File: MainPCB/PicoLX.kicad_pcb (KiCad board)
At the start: 2 copper layers, 120.6 x 70.6 mm, 83 parts, among them J1 USB_C_Receptacle_USB2.0, J2 Conn_01x03, SW1 SW_Push, U1 RP2040, U2 W25Q32JVSS, U3 NCP1117-3.3_SOT223, U4 SN74LV1T34DBV, Y1 12.000MHz

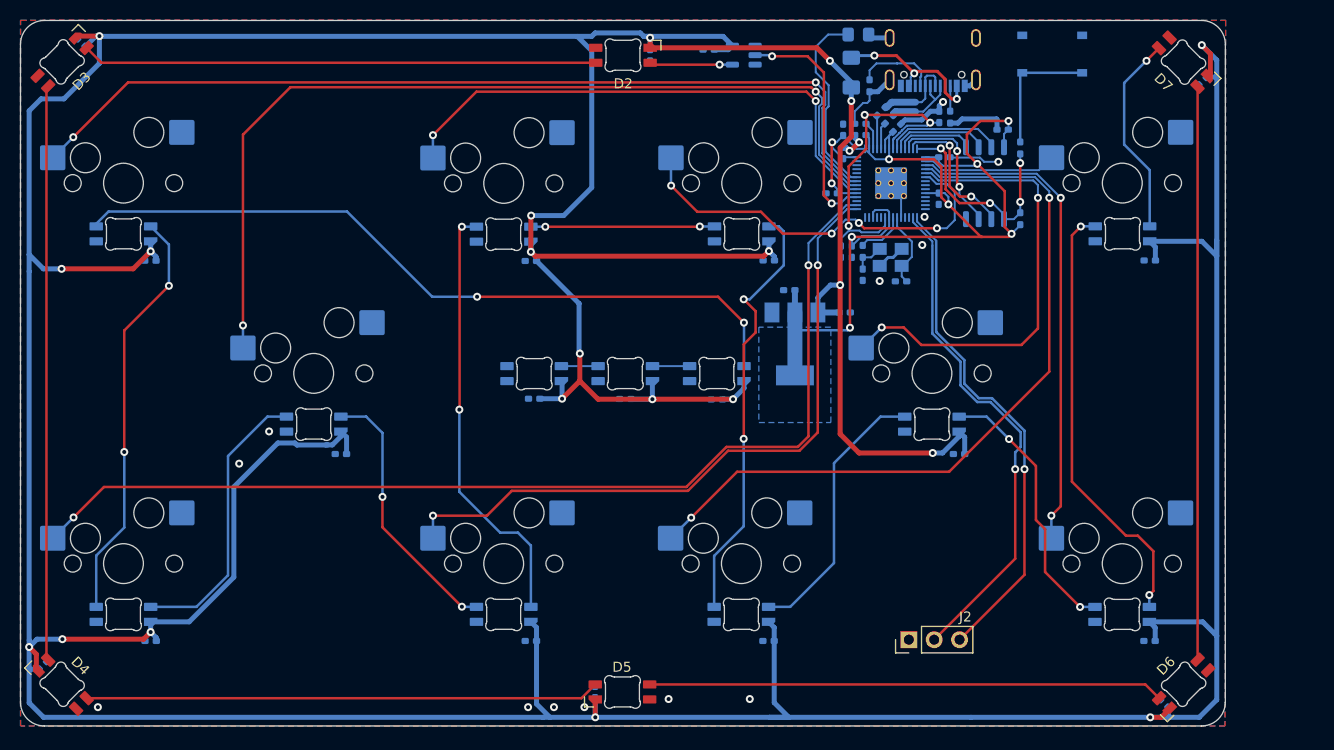
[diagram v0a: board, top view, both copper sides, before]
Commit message: fancy plate graphics, reroute all the LEDs because wrong pinout
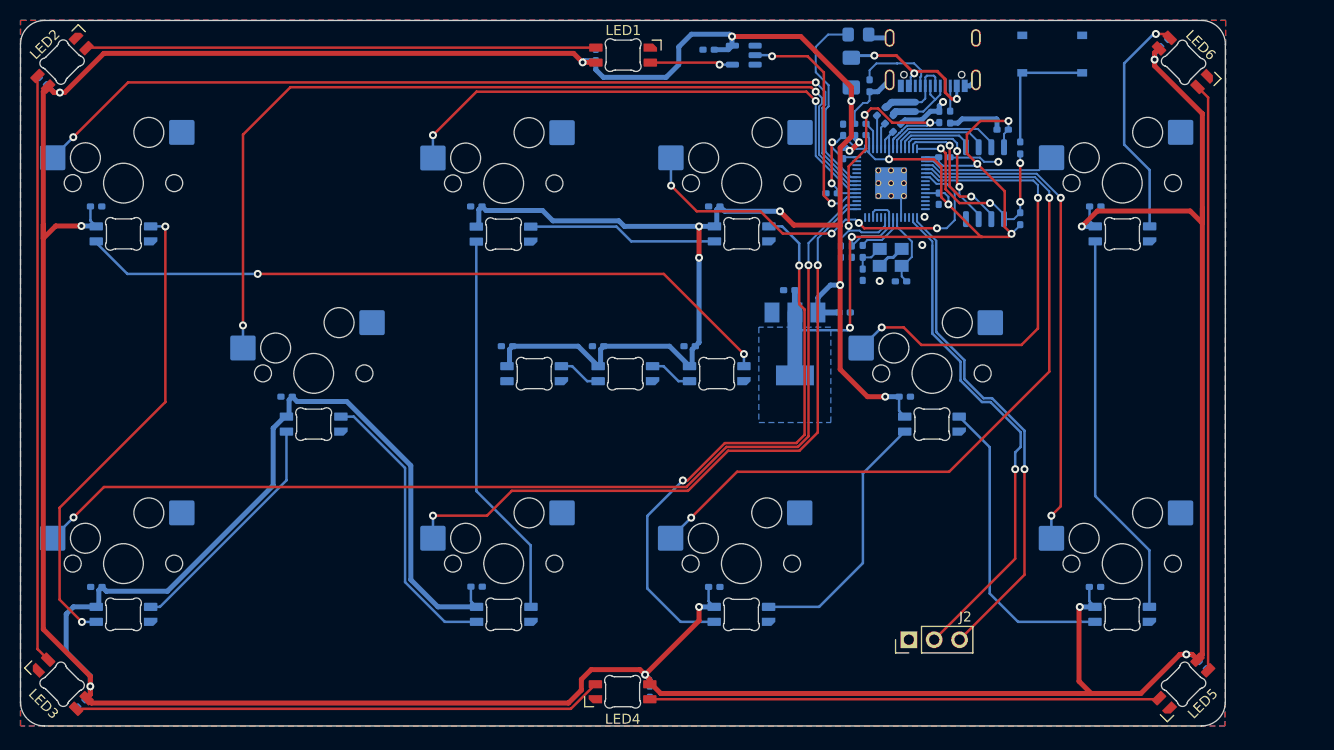
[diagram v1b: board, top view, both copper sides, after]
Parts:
- removed D10, D11, D12, D13, D14, D15, D16, D17, D18, D19, D2, D20, D3, D4, D5, D6, D7, D8, D9: SK6812MINI, marbastlib-various:LED_6028R
- added LED1: SK6812MINI-E, marbastlib-various:LED_6028R, F.Cu at (159.4, 64.5)
- added LED10: SK6812MINI-E, marbastlib-various:LED_6028R, B.Cu at (171.2, 120.5)
- added LED11: SK6812MINI-E, marbastlib-various:LED_6028R, B.Cu at (171.2, 82.3)
- added LED12: SK6812MINI-E, marbastlib-various:LED_6028R, B.Cu at (147.4, 82.4)
- added LED13: SK6812MINI-E, marbastlib-various:LED_6028R, B.Cu at (147.4, 120.5)
- added LED14: SK6812MINI-E, marbastlib-various:LED_6028R, B.Cu at (128.4, 101.4)
- added LED15: SK6812MINI-E, marbastlib-various:LED_6028R, B.Cu at (109.3, 120.5)
- added LED16: SK6812MINI-E, marbastlib-various:LED_6028R, B.Cu at (109.3, 82.3)
- added LED17: SK6812MINI-E, marbastlib-various:LED_6028R, B.Cu at (168.8, 96.3)
- added LED18: SK6812MINI-E, marbastlib-various:LED_6028R, B.Cu at (159.6, 96.3)
- added LED19: SK6812MINI-E, marbastlib-various:LED_6028R, B.Cu at (150.5, 96.3)
- added LED2: SK6812MINI-E, marbastlib-various:LED_6028R, F.Cu at (103.2, 65.1)
- added LED3: SK6812MINI-E, marbastlib-various:LED_6028R, F.Cu at (103.2, 127.5)
- added LED4: SK6812MINI-E, marbastlib-various:LED_6028R, F.Cu at (159.3, 128.2)
- added LED5: SK6812MINI-E, marbastlib-various:LED_6028R, F.Cu at (215.5, 127.5)
- added LED6: SK6812MINI-E, marbastlib-various:LED_6028R, F.Cu at (215.5, 65.2)
- added LED7: SK6812MINI-E, marbastlib-various:LED_6028R, B.Cu at (209.4, 82.3)
- added LED8: SK6812MINI-E, marbastlib-various:LED_6028R, B.Cu at (209.3, 120.5)
- added LED9: SK6812MINI-E, marbastlib-various:LED_6028R, B.Cu at (190.3, 101.4)
- moved C31 7.91 mm to (125.7, 98.7)
- moved C26 7.91 mm to (187.6, 98.7), turned to 0 degrees
- moved C29 7.72 mm to (144.7, 79.6)
- moved C25 7.69 mm to (206.6, 117.7), turned to 0 degrees
- moved C24 7.69 mm to (206.7, 79.6), turned to 0 degrees
- moved C27 7.69 mm to (168.5, 79.6)
- moved C30 7.69 mm to (144.7, 117.7), turned to 180 degrees
- moved C33 7.69 mm to (106.6, 79.6), turned to 180 degrees
- moved C32 7.67 mm to (106.6, 117.7)
- moved C28 7.67 mm to (168.5, 117.7), turned to 0 degrees
- moved C34 5.99 mm to (166.0, 93.6)
- moved C35 5.94 mm to (156.9, 93.6)
- moved C36 5.92 mm to (147.8, 93.6)
- moved C21 5.49 mm to (162.1, 128.2), turned to 90 degrees
- moved C19 5.46 mm to (101.3, 67.1)
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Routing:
- net Net-(LED2-DOUT): track 0.00 -> 58.9 mm
- net Net-(LED5-DOUT): track 0.00 -> 58.9 mm
- net Net-(LED10-DOUT): track 0.00 -> 57.6 mm, vias 0 -> 2
- net Net-(D3-DOUT): track 57.6 -> 0.00 mm
- net Net-(D6-DOUT): track 57.4 -> 0.00 mm
- net Net-(LED3-DOUT): track 0.00 -> 53.0 mm
- net Net-(D2-DOUT): track 51.6 -> 0.00 mm
- net Net-(D5-DOUT): track 51.6 -> 0.00 mm
- net Net-(D4-DOUT): track 51.5 -> 0.00 mm
- net Net-(LED4-DOUT): track 0.00 -> 51.0 mm
- net Net-(LED1-DOUT): track 0.00 -> 51.0 mm
- net Net-(LED15-DOUT): track 0.00 -> 47.8 mm, vias 0 -> 2
- net Net-(D16-DOUT): track 44.2 -> 0.00 mm, vias 2 -> 0
- net Net-(D11-DOUT): track 43.6 -> 0.00 mm, vias 2 -> 0
- net Net-(D13-DOUT): track 43.5 -> 0.00 mm, vias 2 -> 0
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
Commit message: Move buttons, add totally 100% real LEDs to plate
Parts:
- removed J2: Conn_01x03, Connector_PinHeader_2.54mm:PinHeader_1x03_P2.54mm_Vertical
- added SW2: Test, Button_Switch_THT:SW_Tactile_SPST_Angled_PTS645Vx39-2LFS, F.Cu at (225.5, 99.3)
- added SW3: Service, Button_Switch_THT:SW_Tactile_SPST_Angled_PTS645Vx39-2LFS, F.Cu at (225.6, 88.7)
- moved C6 0.21 mm to (183.1, 72.2)
- moved C3 0.21 mm to (183.1, 71.1)
- moved C13 0.18 mm to (181.4, 71.8)
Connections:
- U1 pad 15: TEST -> SERVICE
- U1 pad 16: SERVICE -> TEST
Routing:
- net SERVICE: track 50.8 -> 42.6 mm, vias 1 -> 2
- net +5V: track 604.0 -> 600.6 mm
- net Net-(D1-A): track 19.1 -> 16.9 mm
- net TEST: track 49.9 -> 51.3 mm, vias 1 -> 2
- net P1 UL: track 91.8 -> 93.0 mm
- net +1V1: track 36.5 -> 37.2 mm
- net QSPI_SS: track 21.8 -> 21.1 mm
- net P2 UL: track 40.8 -> 41.5 mm
- net GND: track 34.9 -> 34.7 mm, vias 7 -> 6
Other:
- board size 120.6 x 70.6 mm -> 129.5 x 70.6 mm

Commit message: Update README, generate gerbers, minor fixes
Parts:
- removed F1: 500mA, Fuse:Fuse_1206_3216Metric_Pad1.42x1.75mm_HandSolder
- added R2: DNF, Resistor_SMD:R_0402_1005Metric_Pad0.72x0.64mm_HandSolder, B.Cu at (179.9, 63.0)
- C18, C19, C20, C21, C22, C23, C24, C25, C26, C27, C28, C29, C30, C31, C32, C33, C34, C35, C36: footprint Capacitor_SMD:C_0402_1005Metric_Pad0.74x0.62mm_HandSolder -> Capacitor_SMD:C_0805_2012Metric_Pad1.18x1.45mm_HandSolder
- D1: value LED_Small -> DNF
- moved C17 4.78 mm to (172.4, 62.2), turned to 180 degrees
- moved C22 4.23 mm to (213.2, 125.2), turned to 45 degrees
- moved C20 4.20 mm to (105.5, 125.2), turned to 135 degrees
- moved C21 4.20 mm to (159.3, 125.0), turned to 0 degrees
- moved C18 4.16 mm to (159.4, 67.6), turned to 0 degrees
- moved C19 4.15 mm to (105.4, 67.4), turned to -135 degrees
- moved C23 4.07 mm to (213.4, 67.3), turned to 135 degrees
- moved C24 3.90 mm to (203.8, 82.2), turned to -90 degrees
- moved C30 3.90 mm to (142.2, 120.7), turned to 90 degrees
- moved C29 3.12 mm to (141.6, 79.6)
- moved C31 3.12 mm to (122.6, 98.7)
- moved C32 3.12 mm to (103.5, 117.7)
- moved C33 3.09 mm to (103.5, 79.6), turned to 0 degrees
- moved C25 3.09 mm to (203.5, 117.7), turned to 180 degrees
- moved C26 3.09 mm to (184.5, 98.7), turned to 180 degrees
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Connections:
- J1 pad A4: Net-(F1-Pad1) -> +5V
- J1 pad A9: Net-(F1-Pad1) -> +5V
- J1 pad B4: Net-(F1-Pad1) -> +5V
- J1 pad B9: Net-(F1-Pad1) -> +5V
- U1 pad 37: Net-(D1-A) -> Net-(U1-GPIO25)
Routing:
- net +5V: track 600.6 -> 623.1 mm, vias 17 -> 18
- net Net-(F1-Pad1): track 16.2 -> 0.00 mm, vias 3 -> 0
- net Net-(D1-A): track 16.9 -> 1.97 mm
- net Net-(U1-GPIO25): track 0.00 -> 14.8 mm
- net Net-(LED10-DOUT): track 57.1 -> 60.1 mm
- net Net-(LED13-DOUT): track 28.8 -> 29.3 mm

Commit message: Finalize main PCB design, include design files (JLC)
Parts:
- moved C17 5.60 mm to (170.5, 67.4)
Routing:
- net +5V: track 623.1 -> 627.2 mm
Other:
- board text added: "BEYOND EVOLUTION"
- board text added: "HEY! Why don't you just get up and dance, man?"
- board text added: "SERVICE"
- board text added: "TEST"
- board text added: "by dj505"
